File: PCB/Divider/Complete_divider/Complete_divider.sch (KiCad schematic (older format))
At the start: 0 parts

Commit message: Small modifications
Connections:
- no-connect marks 0 -> 7
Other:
- note added: "Grids 1,2,3 &\nMid. electrodes\n"
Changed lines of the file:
@@
 $EndDescr
 $Sheet
-S 3250 4350 2850 2200
+S 6200 3900 2450 400
+U 5E63EFA9
+F0 "Schematics for Divider2" 50
+F1 "Divider2.sch" 50
+F2 "Pwr_in" I L 6200 4100 50
+F3 "To_Ap_grid" O R 8650 4100 50
+$EndSheet
+Wire Wire Line
+	3600 4150 3750 4150
+Wire Wire Line
+	3750 4150 3750 2550
+Wire Wire Line
+	3750 2550 3950 2550
+Wire Wire Line
+	4750 3000 6150 3000
+Wire Wire Line
+	6150 3000 6150 1850
+Wire Wire Line
+	6150 1850 6000 1850
+Wire Wire Line
+	4750 3000 4750 4000
+Wire Wire Line
+	4950 3050 6200 3050
+Wire Wire Line
+	6200 2050 6000 2050
+Wire Wire Line
+	5150 3100 6250 3100
+Wire Wire Line
+	6250 2250 6000 2250
+Wire Wire Line
+	6000 2650 6050 2650
+Wire Wire Line
+	6050 4100 6200 4100
+$Sheet
+S 1150 3950 2450 400
+U 5E6FA86A
+F0 "Schematics for Divider1" 50
+F1 "Divider1.sch" 50
+F2 "15kV_in" I L 1150 4150 50
+F3 "To_Grid" O R 3600 4150 50
+$EndSheet
+Wire Wire Line
+	6000 1500 6100 1500
+Wire Wire Line
+	6100 1500 6100 1200
+Wire Wire Line
+	6100 1200 1000 1200
+Wire Wire Line
+	1000 1200 1000 4150
+Wire Wire Line
+	1000 4150 1150 4150
+NoConn ~ 5150 4000
+NoConn ~ 4950 4000
+NoConn ~ 4750 4000
+Text Notes 4450 4400 0    98   ~ 0
+Grids 1,2,3 &\nMid. electrodes\n
+$Sheet
+S 3950 1400 2050 1400
 U 5E63F098
 F0 "Schematics for Alim_and_ctr" 50
 F1 "Alim_and_ctr.sch" 50
+F2 "Grid1" O R 6000 1850 50
+F3 "Grid2" O R 6000 2050 50
+F4 "Grid3" O R 6000 2250 50
+F5 "Electrode_in" I L 3950 2550 50
+F6 "Electrode_out" O R 6000 2650 50
+F7 "Pwr_out" O R 6000 1500 50
+F8 "Middle_electrode1" O R 6000 1700 50
+F9 "Middle_electrode2" O R 6000 2400 50
+F10 "Needle" O R 6000 1600 50
 $EndSheet
-$Sheet
-S 2850 1450 2400 2150
-U 5E6FA86A
-F0 "Schematics for Divider1" 50
-F1 "Divider1.sch" 50
-$EndSheet
-$Sheet
-S 6650 1800 2450 2150
-U 5E63EFA9
-F0 "Schematics for Divider2" 50
-F1 "Divider2.sch" 50
-$EndSheet
+Wire Wire Line
+	6300 3150 5450 3150
+Wire Wire Line
+	6000 2400 6300 2400
+Wire Wire Line
+	6200 2050 6200 3050
+Wire Wire Line
+	6300 2400 6300 3150
+Wire Wire Line
+	6250 3100 6250 2250
+Wire Wire Line
+	4450 4000 4450 2950
+Wire Wire Line
+	4450 2950 6100 2950
+Wire Wire Line
+	6100 2950 6100 1700
+Wire Wire Line
+	6100 1700 6000 1700
+NoConn ~ 4450 4000
+NoConn ~ 5450 4000
+Wire Wire Line
+	4950 4000 4950 3050
+Wire Wire Line
+	5150 4000 5150 3100
+Wire Wire Line
+	5450 4000 5450 3150
+Wire Wire Line
+	6050 2650 6050 4100
+NoConn ~ 9350 4100
+Wire Wire Line
+	8650 4100 9350 4100
+Wire Wire Line
+	6000 1600 6200 1600
+Wire Wire Line
+	6200 1600 6200 1150
+Wire Wire Line
+	6200 1150 650  1150
+Wire Wire Line
+	650  1150 650  4150
+Wire Wire Line
+	650  4150 700  4150
+NoConn ~ 700  4150
 $EndSCHEMATC

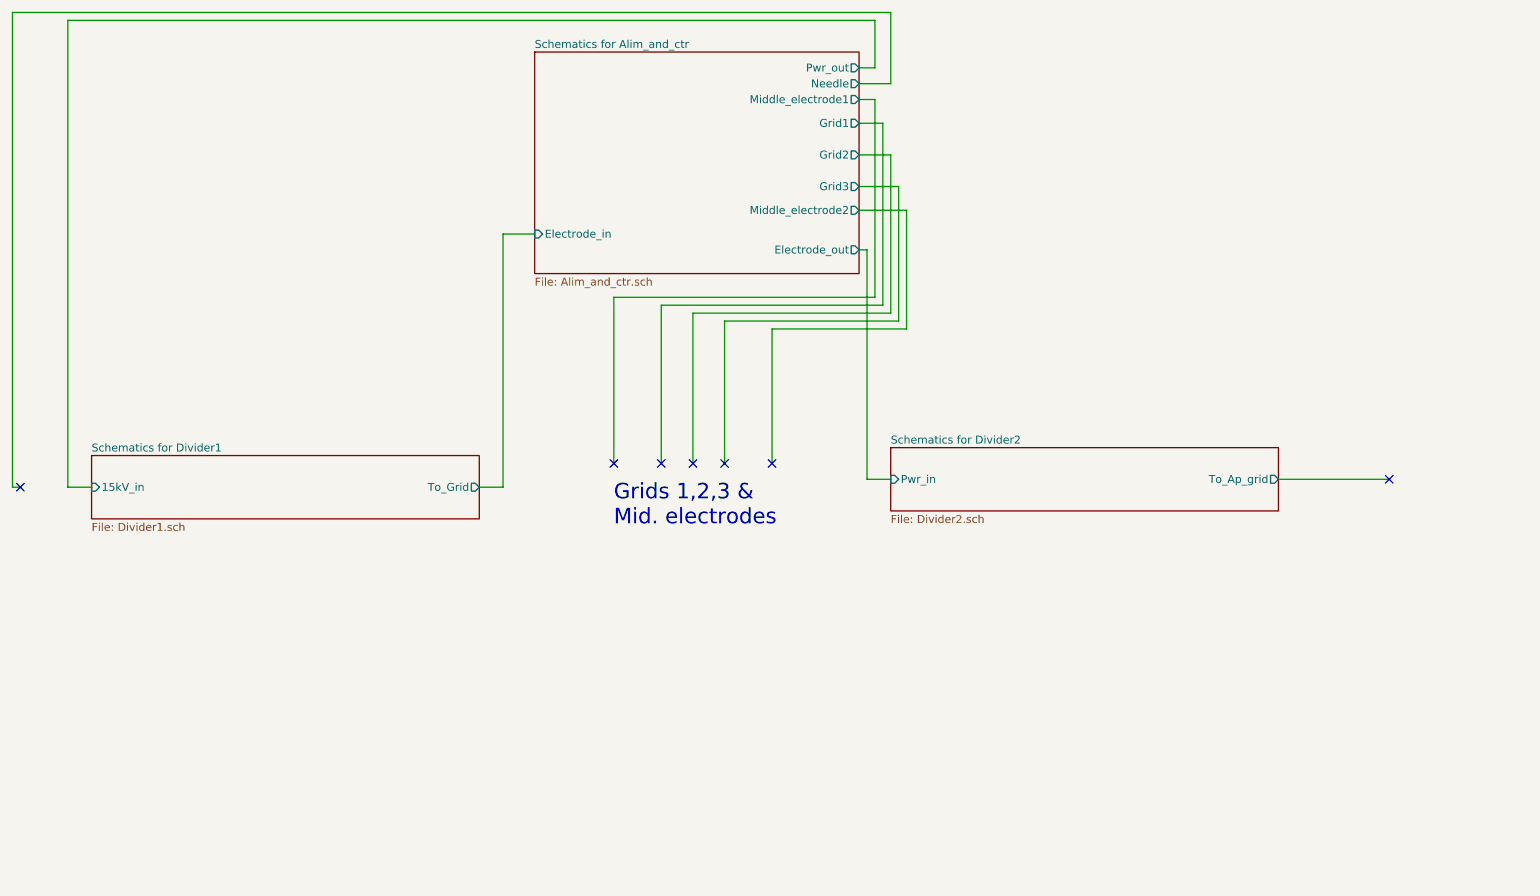
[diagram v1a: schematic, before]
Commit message: DC/DC isolated converter implementation
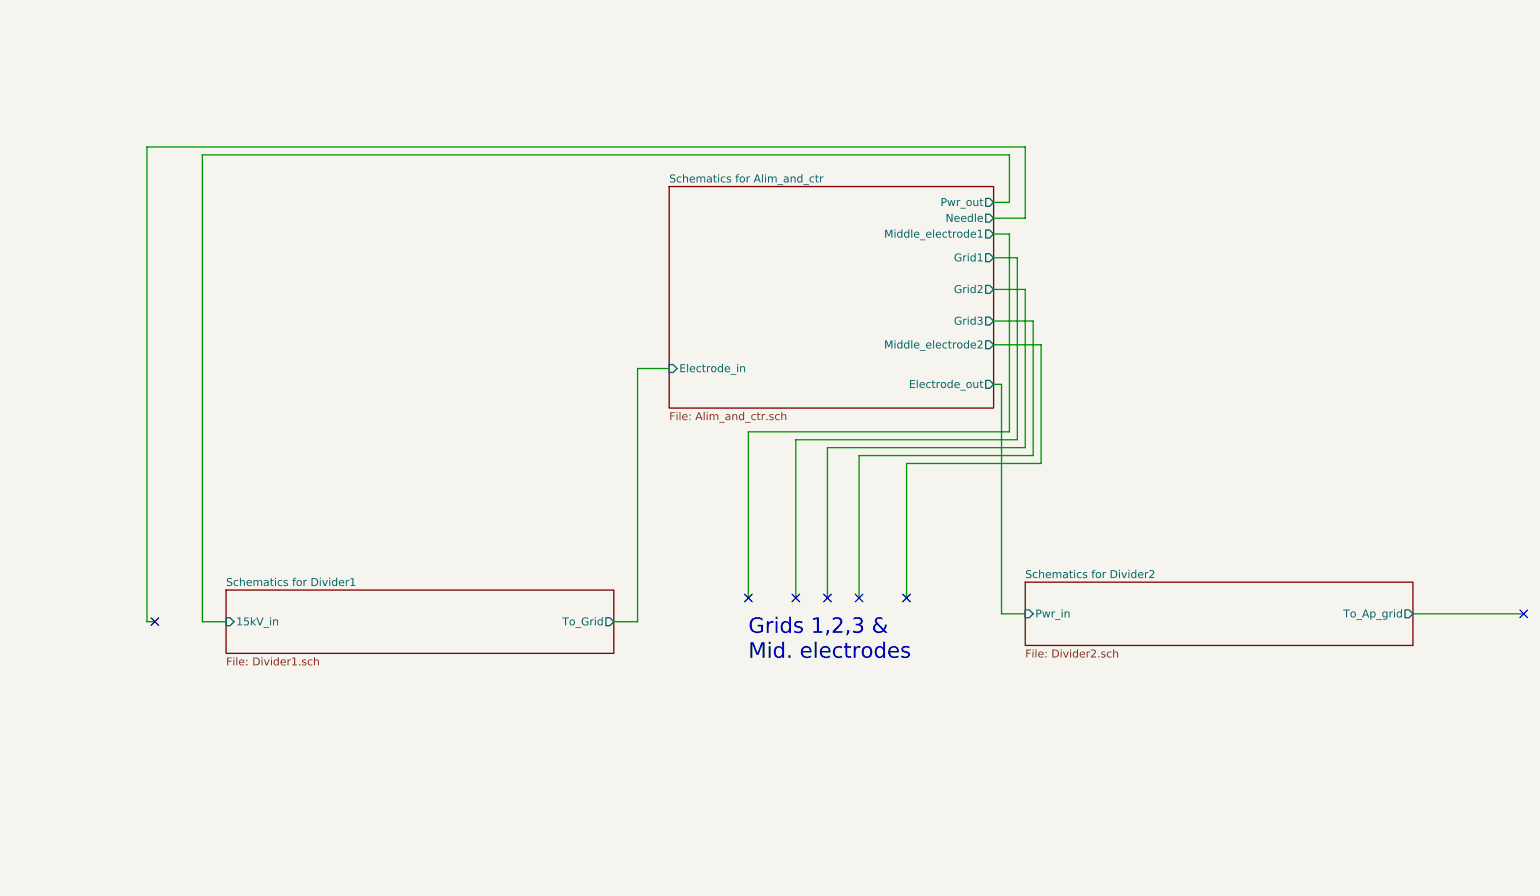
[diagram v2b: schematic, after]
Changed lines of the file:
@@
 $EndDescr
 $Sheet
-S 6200 3900 2450 400
+S 7050 4750 2450 400
 U 5E63EFA9
 F0 "Schematics for Divider2" 50
 F1 "Divider2.sch" 50
-F2 "Pwr_in" I L 6200 4100 50
-F3 "To_Ap_grid" O R 8650 4100 50
+F2 "Pwr_in" I L 7050 4950 50
+F3 "To_Ap_grid" O R 9500 4950 50
 $EndSheet
 Wire Wire Line
-	3600 4150 3750 4150
+	4450 5000 4600 5000
 Wire Wire Line
-	3750 4150 3750 2550
+	4600 5000 4600 3400
 Wire Wire Line
-	3750 2550 3950 2550
+	4600 3400 4800 3400
 Wire Wire Line
-	4750 3000 6150 3000
+	5600 3850 7000 3850
 Wire Wire Line
-	6150 3000 6150 1850
+	7000 3850 7000 2700
 Wire Wire Line
-	6150 1850 6000 1850
+	7000 2700 6850 2700
 Wire Wire Line
-	4750 3000 4750 4000
+	5600 3850 5600 4850
 Wire Wire Line
-	4950 3050 6200 3050
+	5800 3900 7050 3900
 Wire Wire Line
-	6200 2050 6000 2050
+	7050 2900 6850 2900
 Wire Wire Line
-	5150 3100 6250 3100
+	6000 3950 7100 3950
 Wire Wire Line
-	6250 2250 6000 2250
+	7100 3100 6850 3100
 Wire Wire Line
-	6000 2650 6050 2650
+	6850 3500 6900 3500
 Wire Wire Line
-	6050 4100 6200 4100
+	6900 4950 7050 4950
 $Sheet
-S 1150 3950 2450 400
+S 2000 4800 2450 400
 U 5E6FA86A
 F0 "Schematics for Divider1" 50
 F1 "Divider1.sch" 50
-F2 "15kV_in" I L 1150 4150 50
-F3 "To_Grid" O R 3600 4150 50
+F2 "15kV_in" I L 2000 5000 50
+F3 "To_Grid" O R 4450 5000 50
 $EndSheet
 Wire Wire Line
-	6000 1500 6100 1500
+	6850 2350 6950 2350
 Wire Wire Line
-	6100 1500 6100 1200
+	6950 2350 6950 2050
 Wire Wire Line
-	6100 1200 1000 1200
+	6950 2050 1850 2050
 Wire Wire Line
-	1000 1200 1000 4150
+	1850 2050 1850 5000
 Wire Wire Line
-	1000 4150 1150 4150
-NoConn ~ 5150 4000
-NoConn ~ 4950 4000
-NoConn ~ 4750 4000
-Text Notes 4450 4400 0    98   ~ 0
+	1850 5000 2000 5000
+NoConn ~ 6000 4850
+NoConn ~ 5800 4850
+NoConn ~ 5600 4850
+Text Notes 5300 5250 0    98   ~ 0
 Grids 1,2,3 &\nMid. electrodes\n
 $Sheet
-S 3950 1400 2050 1400
+S 4800 2250 2050 1400
 U 5E63F098
 F0 "Schematics for Alim_and_ctr" 50
 F1 "Alim_and_ctr.sch" 50
-F2 "Grid1" O R 6000 1850 50
-F3 "Grid2" O R 6000 2050 50
-F4 "Grid3" O R 6000 2250 50
-F5 "Electrode_in" I L 3950 2550 50
-F6 "Electrode_out" O R 6000 2650 50
-F7 "Pwr_out" O R 6000 1500 50
-F8 "Middle_electrode1" O R 6000 1700 50
-F9 "Middle_electrode2" O R 6000 2400 50
-F10 "Needle" O R 6000 1600 50
+F2 "Grid1" O R 6850 2700 50
+F3 "Grid2" O R 6850 2900 50
+F4 "Grid3" O R 6850 3100 50
+F5 "Electrode_in" I L 4800 3400 50
+F6 "Electrode_out" O R 6850 3500 50
+F7 "Pwr_out" O R 6850 2350 50
+F8 "Middle_electrode1" O R 6850 2550 50
+F9 "Middle_electrode2" O R 6850 3250 50
+F10 "Needle" O R 6850 2450 50
 $EndSheet
 Wire Wire Line
-	6300 3150 5450 3150
+	7150 4000 6300 4000
 Wire Wire Line
-	6000 2400 6300 2400
+	6850 3250 7150 3250
 Wire Wire Line
-	6200 2050 6200 3050
+	7050 2900 7050 3900
 Wire Wire Line
-	6300 2400 6300 3150
+	7150 3250 7150 4000
 Wire Wire Line
-	6250 3100 6250 2250
+	7100 3950 7100 3100
 Wire Wire Line
-	4450 4000 4450 2950
+	5300 4850 5300 3800
 Wire Wire Line
-	4450 2950 6100 2950
+	5300 3800 6950 3800
 Wire Wire Line
-	6100 2950 6100 1700
+	6950 3800 6950 2550
 Wire Wire Line
-	6100 1700 6000 1700
-NoConn ~ 4450 4000
-NoConn ~ 5450 4000
+	6950 2550 6850 2550
+NoConn ~ 5300 4850
+NoConn ~ 6300 4850
 Wire Wire Line
-	4950 4000 4950 3050
+	5800 4850 5800 3900
 Wire Wire Line
-	5150 4000 5150 3100
+	6000 4850 6000 3950
 Wire Wire Line
-	5450 4000 5450 3150
+	6300 4850 6300 4000
 Wire Wire Line
-	6050 2650 6050 4100
-NoConn ~ 9350 4100
+	6900 3500 6900 4950
+NoConn ~ 10200 4950
 Wire Wire Line
-	8650 4100 9350 4100
+	9500 4950 10200 4950
 Wire Wire Line
-	6000 1600 6200 1600
+	6850 2450 7050 2450
 Wire Wire Line
-	6200 1600 6200 1150
+	7050 2450 7050 2000
 Wire Wire Line
-	6200 1150 650  1150
+	7050 2000 1500 2000
 Wire Wire Line
-	650  1150 650  4150
+	1500 2000 1500 5000
 Wire Wire Line
-	650  4150 700  4150
-NoConn ~ 700  4150
+	1500 5000 1550 5000
+NoConn ~ 1550 5000
 $EndSCHEMATC

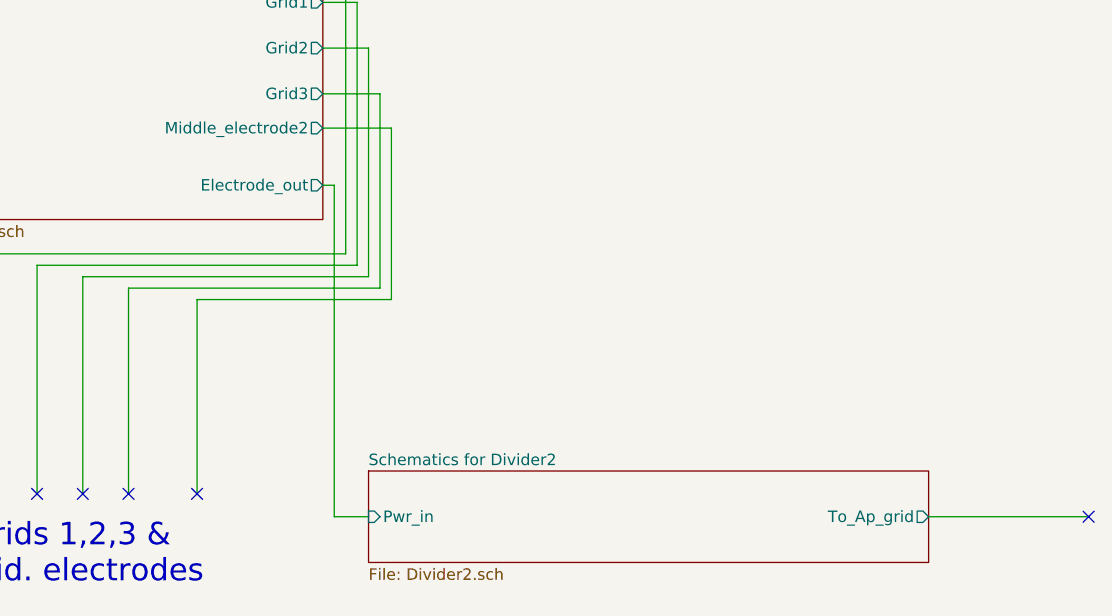
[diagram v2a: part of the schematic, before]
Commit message: Set a Vin of 5V
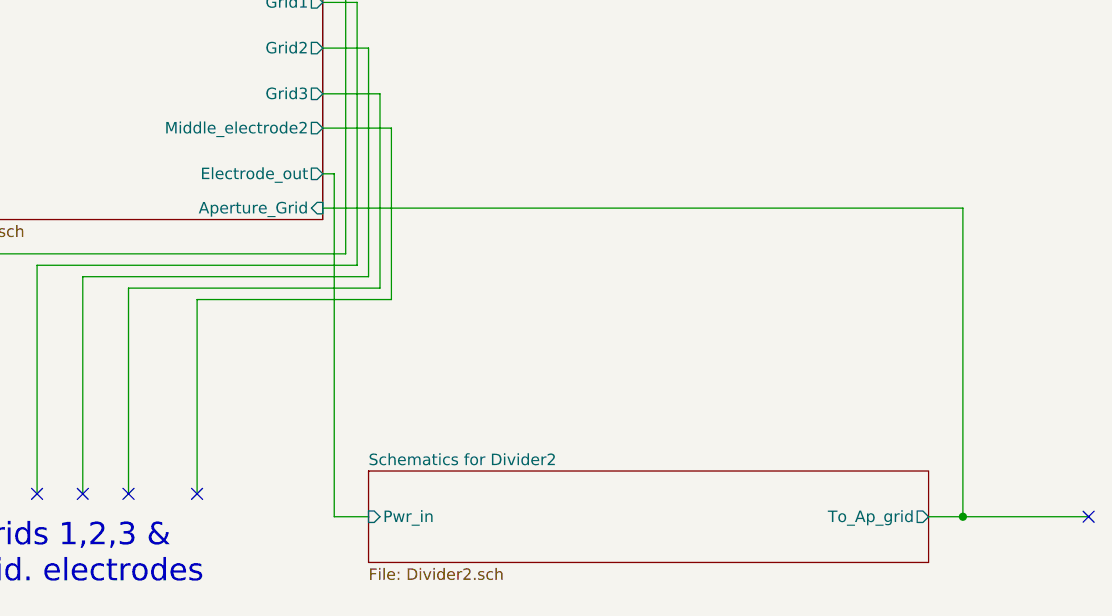
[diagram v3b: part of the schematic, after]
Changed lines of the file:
@@
 	7100 3100 6850 3100
 Wire Wire Line
-	6850 3500 6900 3500
+	6850 3450 6900 3450
 Wire Wire Line
 	6900 4950 7050 4950
@@
 F4 "Grid3" O R 6850 3100 50
 F5 "Electrode_in" I L 4800 3400 50
-F6 "Electrode_out" O R 6850 3500 50
+F6 "Electrode_out" O R 6850 3450 50
 F7 "Pwr_out" O R 6850 2350 50
 F8 "Middle_electrode1" O R 6850 2550 50
 F9 "Middle_electrode2" O R 6850 3250 50
 F10 "Needle" O R 6850 2450 50
+F11 "Aperture_Grid" I R 6850 3600 50
 $EndSheet
 Wire Wire Line
@@
 	6300 4850 6300 4000
 Wire Wire Line
-	6900 3500 6900 4950
+	6900 3450 6900 4950
 NoConn ~ 10200 4950
 Wire Wire Line
-	9500 4950 10200 4950
+	9500 4950 9650 4950
 Wire Wire Line
 	6850 2450 7050 2450
@@
 	1500 5000 1550 5000
 NoConn ~ 1550 5000
+Wire Wire Line
+	6850 3600 9650 3600
+Wire Wire Line
+	9650 3600 9650 4950
+Connection ~ 9650 4950
+Wire Wire Line
+	9650 4950 10200 4950
 $EndSCHEMATC

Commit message: Begin PCB design
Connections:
- no-connect marks 7 -> 5
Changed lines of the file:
@@
 	4600 3400 4800 3400
-Wire Wire Line
-	5600 3850 7000 3850
-Wire Wire Line
-	7000 3850 7000 2700
-Wire Wire Line
-	7000 2700 6850 2700
-Wire Wire Line
-	5600 3850 5600 4850
 Wire Wire Line
 	5800 3900 7050 3900
 Wire Wire Line
 	7050 2900 6850 2900
-Wire Wire Line
-	6000 3950 7100 3950
-Wire Wire Line
-	7100 3100 6850 3100
 Wire Wire Line
 	6850 3450 6900 3450
@@
 $EndSheet
 Wire Wire Line
-	6850 2350 6950 2350
-Wire Wire Line
-	6950 2350 6950 2050
-Wire Wire Line
-	6950 2050 1850 2050
-Wire Wire Line
 	1850 2050 1850 5000
 Wire Wire Line
 	1850 5000 2000 5000
-NoConn ~ 6000 4850
 NoConn ~ 5800 4850
-NoConn ~ 5600 4850
 Text Notes 5300 5250 0    98   ~ 0
 Grids 1,2,3 &\nMid. electrodes\n
-$Sheet
-S 4800 2250 2050 1400
-U 5E63F098
-F0 "Schematics for Alim_and_ctr" 50
-F1 "Alim_and_ctr.sch" 50
-F2 "Grid1" O R 6850 2700 50
-F3 "Grid2" O R 6850 2900 50
-F4 "Grid3" O R 6850 3100 50
-F5 "Electrode_in" I L 4800 3400 50
-F6 "Electrode_out" O R 6850 3450 50
-F7 "Pwr_out" O R 6850 2350 50
-F8 "Middle_electrode1" O R 6850 2550 50
-F9 "Middle_electrode2" O R 6850 3250 50
-F10 "Needle" O R 6850 2450 50
-F11 "Aperture_Grid" I R 6850 3600 50
-$EndSheet
 Wire Wire Line
 	7150 4000 6300 4000
@@
 Wire Wire Line
 	7150 3250 7150 4000
-Wire Wire Line
-	7100 3950 7100 3100
 Wire Wire Line
 	5300 4850 5300 3800
@@
 	5800 4850 5800 3900
 Wire Wire Line
-	6000 4850 6000 3950
-Wire Wire Line
 	6300 4850 6300 4000
 Wire Wire Line
@@
 Wire Wire Line
 	9500 4950 9650 4950
-Wire Wire Line
-	6850 2450 7050 2450
-Wire Wire Line
-	7050 2450 7050 2000
 Wire Wire Line
 	7050 2000 1500 2000
@@
 Wire Wire Line
 	9650 4950 10200 4950
+Wire Wire Line
+	6850 2350 7050 2350
+Wire Wire Line
+	7050 2350 7050 2000
+Wire Wire Line
+	1850 2050 7000 2050
+Wire Wire Line
+	7000 2050 7000 2450
+Wire Wire Line
+	7000 2450 6850 2450
+$Sheet
+S 4800 2250 2050 1400
+U 5E63F098
+F0 "Schematics for Alim_and_ctr" 50
+F1 "Alim_and_ctr.sch" 50
+F2 "Gate" O R 6850 2900 50
+F3 "Electrode_in" I L 4800 3400 50
+F4 "Electrode_out" O R 6850 3450 50
+F5 "Pwr_out" O R 6850 2450 50
+F6 "Middle_electrode1" O R 6850 2550 50
+F7 "Middle_electrode2" O R 6850 3250 50
+F8 "Needle" O R 6850 2350 50
+F9 "Aperture_Grid" I R 6850 3600 50
+$EndSheet
 $EndSCHEMATC

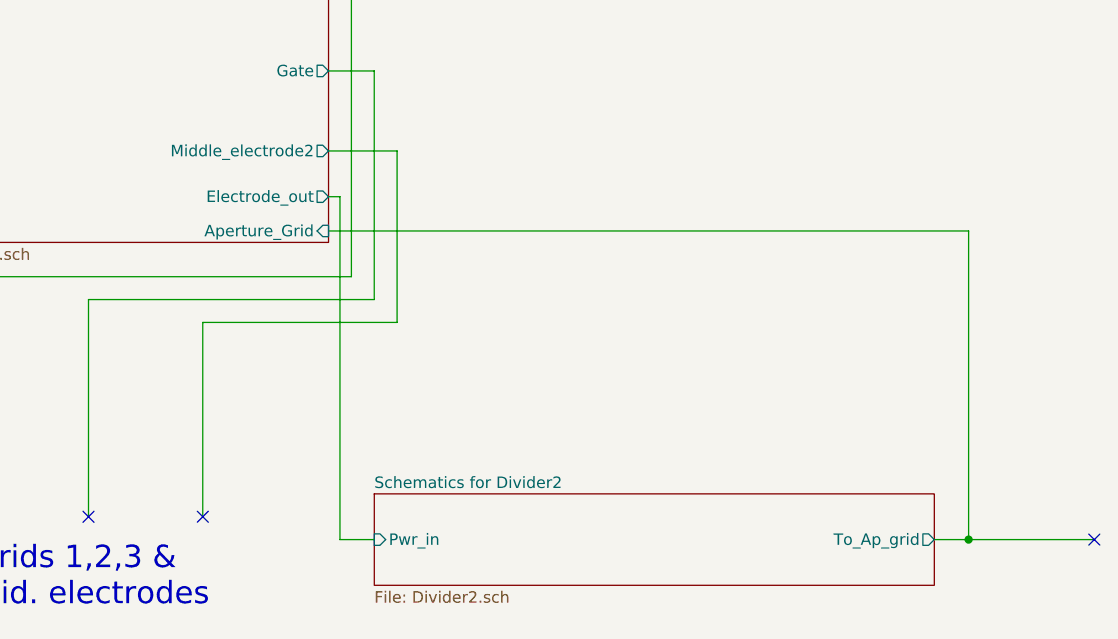
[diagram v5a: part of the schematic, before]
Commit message: HV design finished
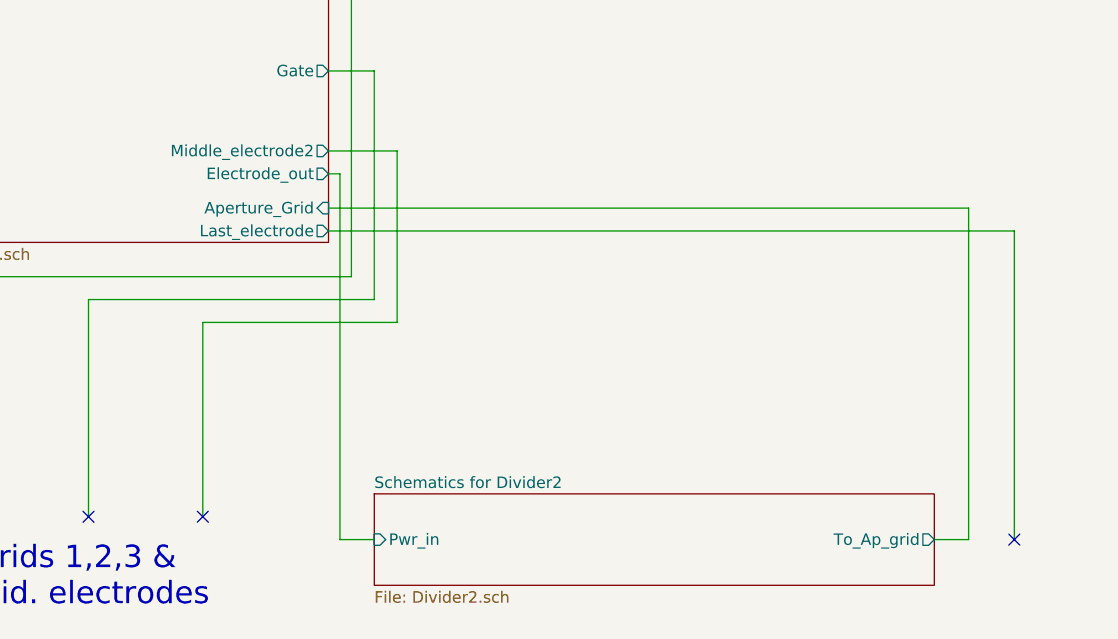
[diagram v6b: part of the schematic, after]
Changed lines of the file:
@@
 	7050 2900 6850 2900
 Wire Wire Line
-	6850 3450 6900 3450
+	6850 3350 6900 3350
 Wire Wire Line
 	6900 4950 7050 4950
@@
 	6300 4850 6300 4000
 Wire Wire Line
-	6900 3450 6900 4950
-NoConn ~ 10200 4950
+	6900 3350 6900 4950
 Wire Wire Line
 	9500 4950 9650 4950
@@
 NoConn ~ 1550 5000
 Wire Wire Line
-	6850 3600 9650 3600
+	6850 3500 9650 3500
 Wire Wire Line
-	9650 3600 9650 4950
-Connection ~ 9650 4950
-Wire Wire Line
-	9650 4950 10200 4950
+	9650 3500 9650 4950
 Wire Wire Line
 	6850 2350 7050 2350
@@
 F2 "Gate" O R 6850 2900 50
 F3 "Electrode_in" I L 4800 3400 50
-F4 "Electrode_out" O R 6850 3450 50
+F4 "Electrode_out" O R 6850 3350 50
 F5 "Pwr_out" O R 6850 2450 50
 F6 "Middle_electrode1" O R 6850 2550 50
 F7 "Middle_electrode2" O R 6850 3250 50
 F8 "Needle" O R 6850 2350 50
-F9 "Aperture_Grid" I R 6850 3600 50
+F9 "Aperture_Grid" I R 6850 3500 50
+F10 "Last_electrode" O R 6850 3600 50
 $EndSheet
+Wire Wire Line
+	6850 3600 9850 3600
+Wire Wire Line
+	9850 3600 9850 4950
+NoConn ~ 9850 4950
 $EndSCHEMATC
